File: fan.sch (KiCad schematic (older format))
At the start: 0 parts

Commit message: Thermocouple and fan
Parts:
- added Q?: MOSFET_N, ~, symbol MOSFET_N
- added R? (x5): R, ~, symbol R
- added U?: LM324, symbol LM324
- added U?: MCP4922-E/P, DIP14, symbol MCP4922-E/P
- added VR?: VR, ~, symbol VR
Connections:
- net Fan_in: now also R?.1, R?.2
- net Power+: now also Q?.S
- new net: R?.2, R?.2, R?.2, U?.3 (+), VR?.1
- new net: R?.1, U?.14 (VoutA)
- new net: R?.1, U?.9 (~SHDN~)
- new net +12V: Q?.D, R?.1, U?.4 (V+)
- new net AGND: R?.2
- new net CS_N: U?.3 (~CS~)
- new net Current Measure: R?.1, U?.2 (-)
- new net MOSI: U?.5 (SDI)
- new net SCLK: U?.4 (SCK)
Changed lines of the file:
@@
 LIBS:contrib
 LIBS:valves
+LIBS:BenchBudEE-cache
 EELAYER 27 0
 EELAYER END
@@
 Sheet 7 8
 Title ""
-Date "27 jan 2014"
+Date "5 feb 2014"
 Rev ""
 Comp ""
@@
 Comment4 ""
 $EndDescr
-Text HLabel 8500 2050 0    60   Output ~ 0
+Text HLabel 8450 2300 2    60   Output ~ 0
 Power+
-Text HLabel 8450 2750 0    60   Input ~ 0
+Text HLabel 8550 3350 2    60   Input ~ 0
 Power-
-Text HLabel 2100 2150 0    60   Output ~ 0
+Text HLabel 1200 4100 0    60   Output ~ 0
 Tach_out
-Text HLabel 1900 2850 0    60   Input ~ 0
+Text HLabel 1000 2400 0    60   Input ~ 0
 Fan_in
-Text HLabel 8500 3650 0    60   Input ~ 0
+Text HLabel 8650 4100 2    60   Input ~ 0
 Tach
+$Comp
+L LM324 U?
+U 1 1 52F2AB7D
+P 5300 2100
+F 0 "U?" H 5350 2300 60  0000 C CNN
+F 1 "LM324" H 5450 1900 50  0000 C CNN
+F 2 "" H 5300 2100 60  0000 C CNN
+F 3 "" H 5300 2100 60  0000 C CNN
+	1    5300 2100
+	1    0    0    -1
+$EndComp
+$Comp
+L MOSFET_N Q?
+U 1 1 52F2AB9B
+P 6600 2100
+F 0 "Q?" H 6610 2270 60  0000 R CNN
+F 1 "MOSFET_N" H 6610 1950 60  0000 R CNN
+F 2 "~" H 6600 2100 60  0000 C CNN
+F 3 "~" H 6600 2100 60  0000 C CNN
+	1    6600 2100
+	1    0    0    -1
+$EndComp
+$Comp
+L R R?
+U 1 1 52F2ABB2
+P 6750 3250
+F 0 "R?" V 6830 3250 40  0000 C CNN
+F 1 "R" V 6757 3251 40  0000 C CNN
+F 2 "~" V 6680 3250 30  0000 C CNN
+F 3 "~" H 6750 3250 30  0000 C CNN
+	1    6750 3250
+	1    0    0    -1
+$EndComp
+Wire Wire Line
+	6750 3000 6750 2750
+$Comp
+L AGND #PWR?
+U 1 1 52F2ABD6
+P 6750 3850
+F 0 "#PWR?" H 6750 3850 40  0001 C CNN
+F 1 "AGND" H 6750 3780 50  0000 C CNN
+F 2 "" H 6750 3850 60  0000 C CNN
+F 3 "" H 6750 3850 60  0000 C CNN
+	1    6750 3850
+	1    0    0    -1
+$EndComp
+Wire Wire Line
+	6750 3500 6750 3850
+$Comp
+L +12V #PWR?
+U 1 1 52F2ABF3
+P 6700 1600
+F 0 "#PWR?" H 6700 1550 20  0001 C CNN
+F 1 "+12V" H 6700 1700 30  0000 C CNN
+F 2 "" H 6700 1600 60  0000 C CNN
+F 3 "" H 6700 1600 60  0000 C CNN
+	1    6700 1600
+	1    0    0    -1
+$EndComp
+Wire Wire Line
+	6700 1900 6700 1600
+Connection ~ 6700 2300
+Wire Wire Line
+	4400 2750 4400 2200
+Wire Wire Line
+	4400 2200 4800 2200
+Connection ~ 6750 2750
+Wire Wire Line
+	8450 2300 6700 2300
+$Comp
+L +12V #PWR?
+U 1 1 52F2AC46
+P 5200 1600
+F 0 "#PWR?" H 5200 1550 20  0001 C CNN
+F 1 "+12V" H 5200 1700 30  0000 C CNN
+F 2 "" H 5200 1600 60  0000 C CNN
+F 3 "" H 5200 1600 60  0000 C CNN
+	1    5200 1600
+	1    0    0    -1
+$EndComp
+Wire Wire Line
+	5200 1700 5200 1600
+$Comp
+L VR VR?
+U 1 1 52F2ACB6
+P 3900 2400
+F 0 "VR?" V 3960 2354 40  0000 C TNN
+F 1 "VR" V 3900 2400 40  0000 C CNN
+F 2 "~" H 3900 2400 60  0000 C CNN
+F 3 "~" H 3900 2400 60  0000 C CNN
+	1    3900 2400
+	1    0    0    -1
+$EndComp
+$Comp
+L R R?
+U 1 1 52F2ACED
+P 3900 1650
+F 0 "R?" V 3980 1650 40  0000 C CNN
+F 1 "R" V 3907 1651 40  0000 C CNN
+F 2 "~" V 3830 1650 30  0000 C CNN
+F 3 "~" H 3900 1650 30  0000 C CNN
+	1    3900 1650
+	1    0    0    -1
+$EndComp
+$Comp
+L +12V #PWR?
+U 1 1 52F2AD0A
+P 3900 1250
+F 0 "#PWR?" H 3900 1200 20  0001 C CNN
+F 1 "+12V" H 3900 1350 30  0000 C CNN
+F 2 "" H 3900 1250 60  0000 C CNN
+F 3 "" H 3900 1250 60  0000 C CNN
+	1    3900 1250
+	1    0    0    -1
+$EndComp
+Wire Wire Line
+	3900 1250 3900 1400
+Wire Wire Line
+	3550 2000 4800 2000
+Connection ~ 3900 2000
+$Comp
+L MCP4922-E/P U?
+U 1 1 52F2ADF1
+P 2000 1250
+F 0 "U?" H 2150 1650 40  0000 L BNN
+F 1 "MCP4922-E/P" H 2150 1600 40  0000 L BNN
+F 2 "DIP14" H 2000 1250 30  0000 C CIN
+F 3 "" H 2000 1250 60  0000 C CNN
+	1    2000 1250
+	1    0    0    -1
+$EndComp
+Text HLabel 1600 2750 0    60   Output ~ 0
+Current Measure
+Connection ~ 4400 2750
+Wire Wire Line
+	6750 2750 1600 2750
+Wire Wire Line
+	3900 1900 3900 2150
+Wire Wire Line
+	1200 4100 8650 4100
+Text HLabel 1000 1050 0    60   Input ~ 0
+MOSI
+Text HLabel 1000 1350 0    60   Output ~ 0
+MISO
+Text HLabel 1000 1250 0    60   Input ~ 0
+CS_N
+Text HLabel 1000 1150 0    60   Input ~ 0
+SCLK
+Wire Wire Line
+	1000 1050 1450 1050
+Wire Wire Line
+	1000 1150 1450 1150
+Wire Wire Line
+	1000 1250 1450 1250
+$Comp
+L R R?
+U 1 1 52F2B0A4
+P 3300 2000
+F 0 "R?" V 3380 2000 40  0000 C CNN
+F 1 "R" V 3307 2001 40  0000 C CNN
+F 2 "~" V 3230 2000 30  0000 C CNN
+F 3 "~" H 3300 2000 30  0000 C CNN
+	1    3300 2000
+	0    -1   -1   0
+$EndComp
+$Comp
+L R R?
+U 1 1 52F2B0B3
+P 3300 2400
+F 0 "R?" V 3380 2400 40  0000 C CNN
+F 1 "R" V 3307 2401 40  0000 C CNN
+F 2 "~" V 3230 2400 30  0000 C CNN
+F 3 "~" H 3300 2400 30  0000 C CNN
+	1    3300 2400
+	0    -1   -1   0
+$EndComp
+Wire Wire Line
+	1000 2400 3050 2400
+Wire Wire Line
+	3550 2400 3700 2400
+Wire Wire Line
+	3700 2400 3700 2000
+Connection ~ 3700 2000
+$Comp
+L R R?
+U 1 1 52F2B10C
+P 1300 1950
+F 0 "R?" V 1380 1950 40  0000 C CNN
+F 1 "R" V 1307 1951 40  0000 C CNN
+F 2 "~" V 1230 1950 30  0000 C CNN
+F 3 "~" H 1300 1950 30  0000 C CNN
+	1    1300 1950
+	1    0    0    -1
+$EndComp
+Wire Wire Line
+	2550 1100 3050 1100
+Wire Wire Line
+	3050 1100 3050 2000
+Wire Wire Line
+	1450 1450 1300 1450
+Wire Wire Line
+	1300 1450 1300 1700
+Wire Wire Line
+	1300 2200 1300 2400
+Connection ~ 1300 2400
 $EndSCHEMATC

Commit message: Arduino
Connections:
- net Current Measure renamed CURR_MEAS
- net Fan_in renamed FAN_EN
- net Power+ renamed FAN_OUT+
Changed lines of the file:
@@
 LIBS:fe_v-
 LIBS:ap5726
+LIBS:arduino_pins
 LIBS:BenchBudEE-cache
 EELAYER 27 0
@@
 Sheet 7 9
 Title ""
-Date "7 feb 2014"
+Date "8 feb 2014"
 Rev ""
 Comp ""
@@
 $EndDescr
 Text HLabel 8450 2300 2    60   Output ~ 0
-Power+
-Text HLabel 8550 3350 2    60   Input ~ 0
-Power-
+FAN_OUT+
+Text HLabel 8500 2750 2    60   Output ~ 0
+FAN_OUT-
 Text HLabel 1200 4100 0    60   Output ~ 0
-Tach_out
+TACH_MEAS
 Text HLabel 1000 2400 0    60   Input ~ 0
-Fan_in
+FAN_EN
 Text HLabel 8650 4100 2    60   Input ~ 0
-Tach
+TACH_IN
 $Comp
 L LM324 U?
@@
 	1    0    0    -1
 $EndComp
-Text HLabel 1600 2750 0    60   Output ~ 0
-Current Measure
+Text HLabel 1200 2750 0    60   Output ~ 0
+CURR_MEAS
 Connection ~ 4400 2750
 Wire Wire Line
-	6750 2750 1600 2750
+	1200 2750 8500 2750
 Wire Wire Line
 	3900 1900 3900 2150

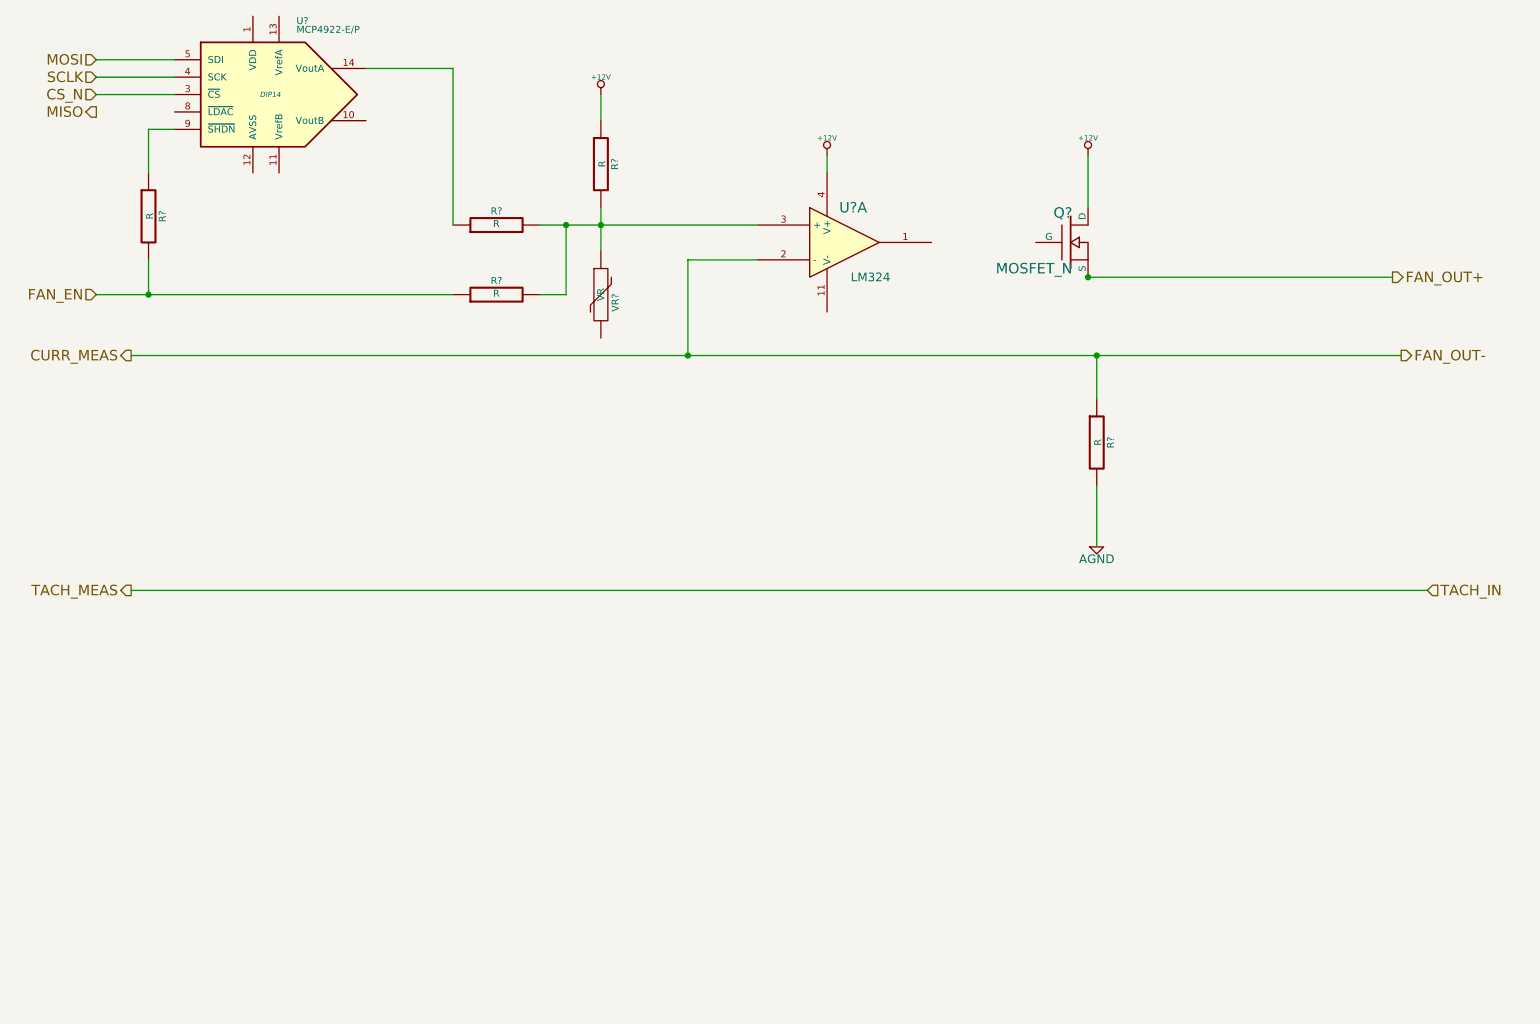
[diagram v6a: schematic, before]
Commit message: Fan/Power refactoring
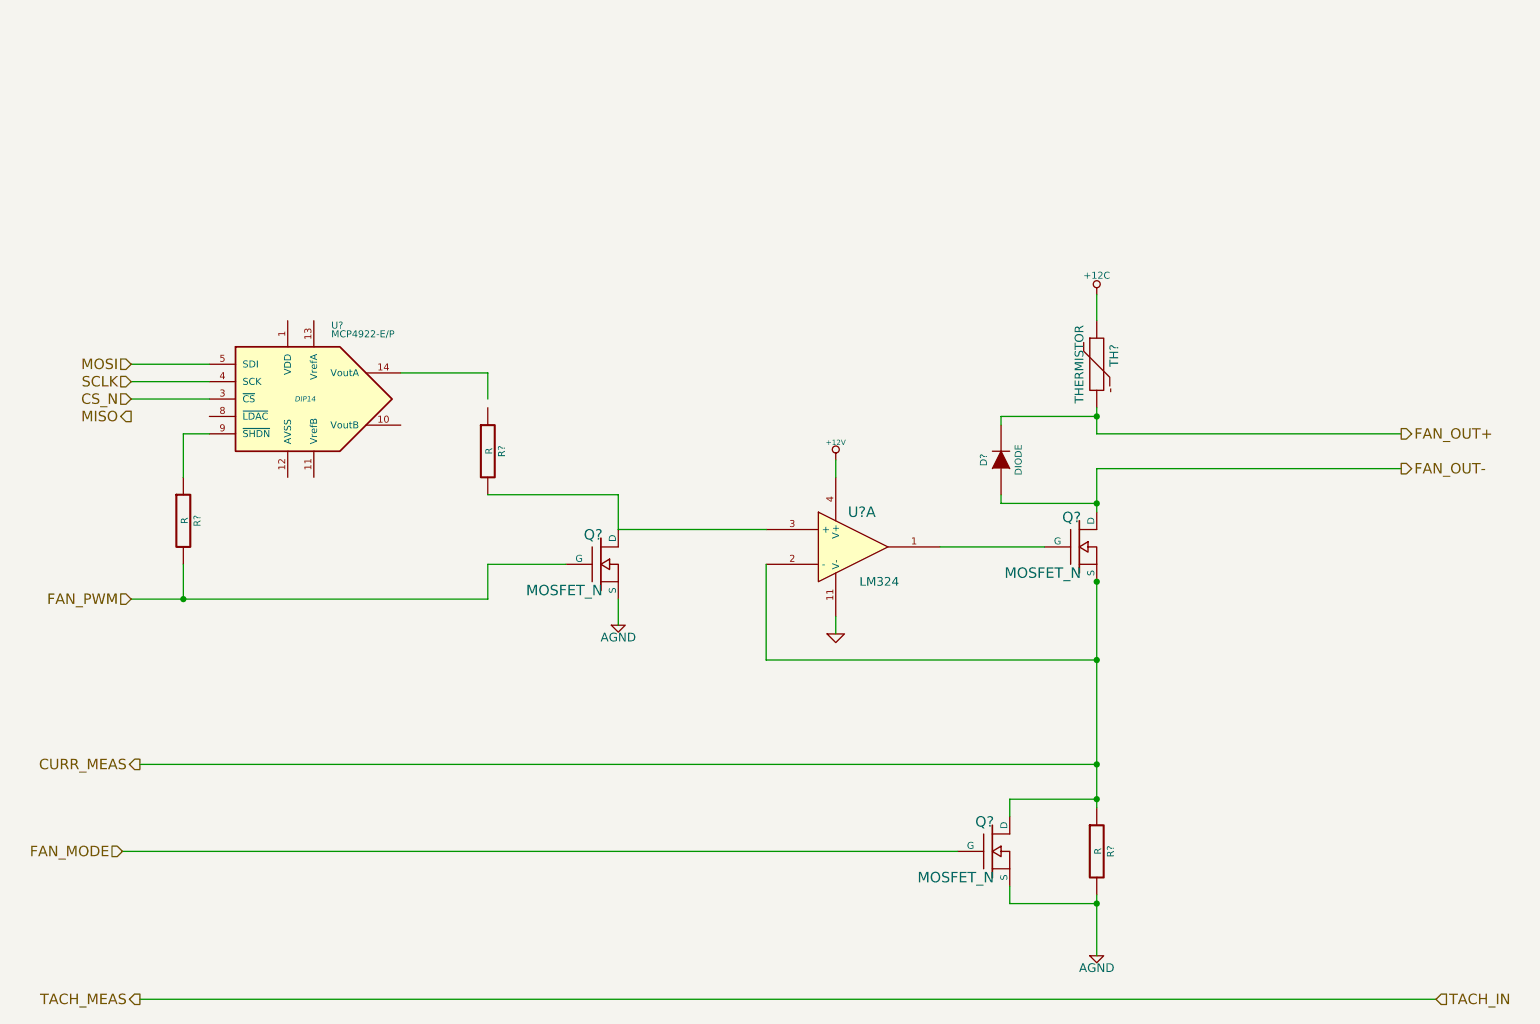
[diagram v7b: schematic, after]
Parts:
- removed R? (x3): R, ~, symbol R
- removed VR?: VR, ~, symbol VR
- added D?: DIODE, ~, symbol DIODE
- added Q? (x2): MOSFET_N, ~, symbol MOSFET_N
- added R?: R, ~, symbol R
- added TH?: THERMISTOR, ~, symbol THERMISTOR
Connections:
- net +12V: no longer Q?.D
- net AGND: now also Q?.S, Q?.S
- net CURR_MEAS: now also Q?.S, Q?.D
- net FAN_OUT+: now also D?.2 (K), TH?.2; no longer Q?.S
- net at U?.1: now also Q?.G
- net GND: now reaches U?.11 (V-)
- net at U?.3 (+): now also Q?.D, R?.2
- net FAN_EN renamed FAN_PWM
- net FAN_PWM: now also Q?.G
- new net +12C: TH?.1
- new net FAN_MODE: Q?.G
- new net FAN_OUT-: D?.1 (A), Q?.D
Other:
- moved on the sheet: Q?, R?, U?, U?A
